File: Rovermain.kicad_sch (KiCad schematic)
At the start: 59 parts, among them J1 48V input, J10 3V3 Output, J11 5V Output, J13 Steering Bus Bar, J14 Drive Bus Bar, J15 Arm Bus Bar, J16 Pi_48V_Ctrl, J17 Spare 48V port, J2 USB_C_Receptacle_Pi_Power, J3 24V Output, J4 USB_C_Receptacle_Spare_power, J5 Buck 48/24, J6 Buck 24/12, J7 Buck 24/5, J8 Buck 12/3v3, J9 12V Output, Q1 Arm ctrl, Q2 Steer ctrl, Q3 Drive ctrl, Q4 Spare ctrl, SW2 SW_Push_Open

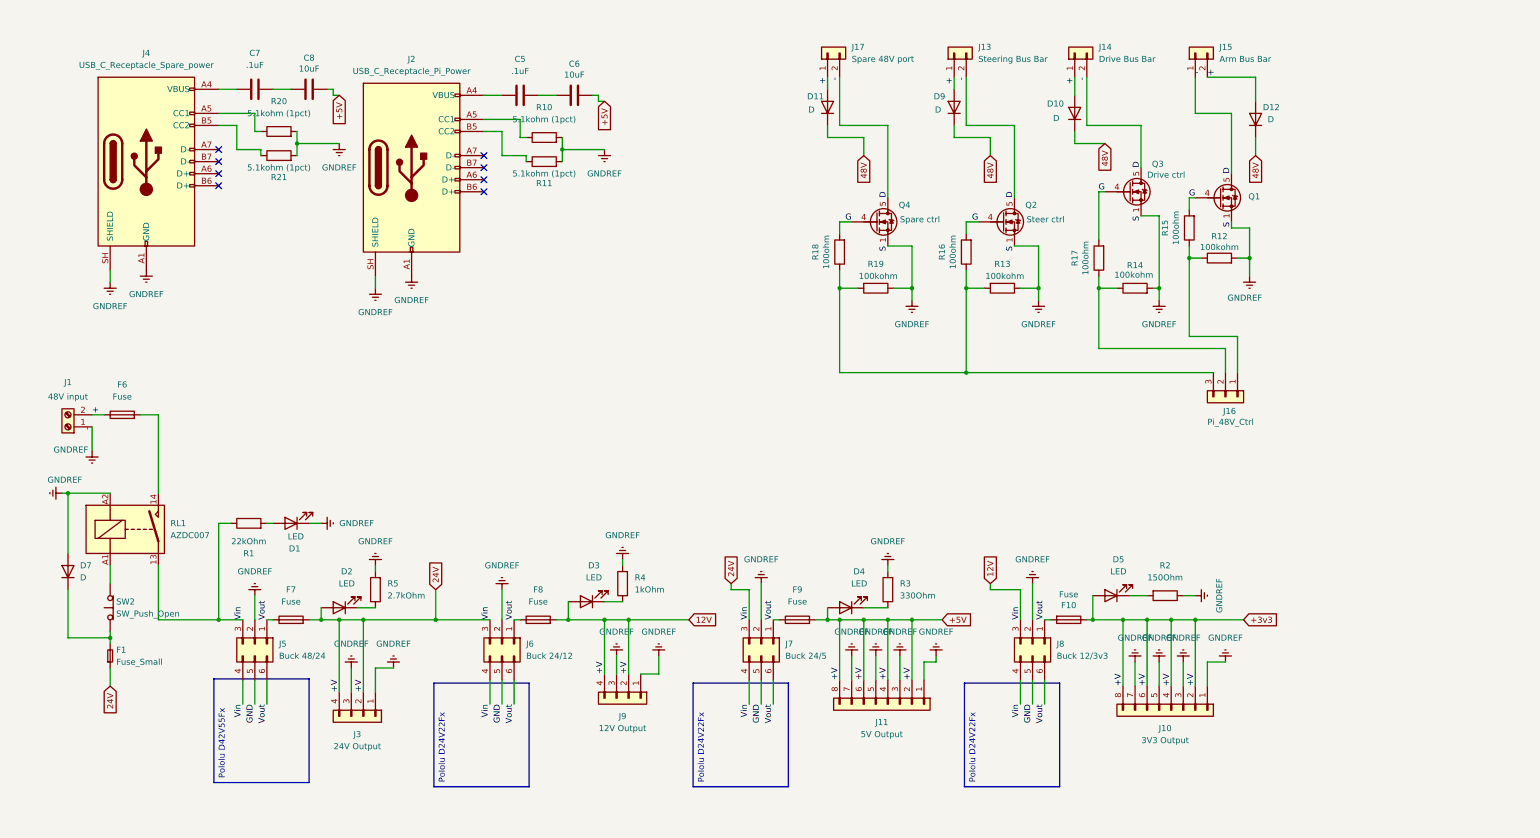
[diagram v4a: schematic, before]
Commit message: finalizing footprints, created layout
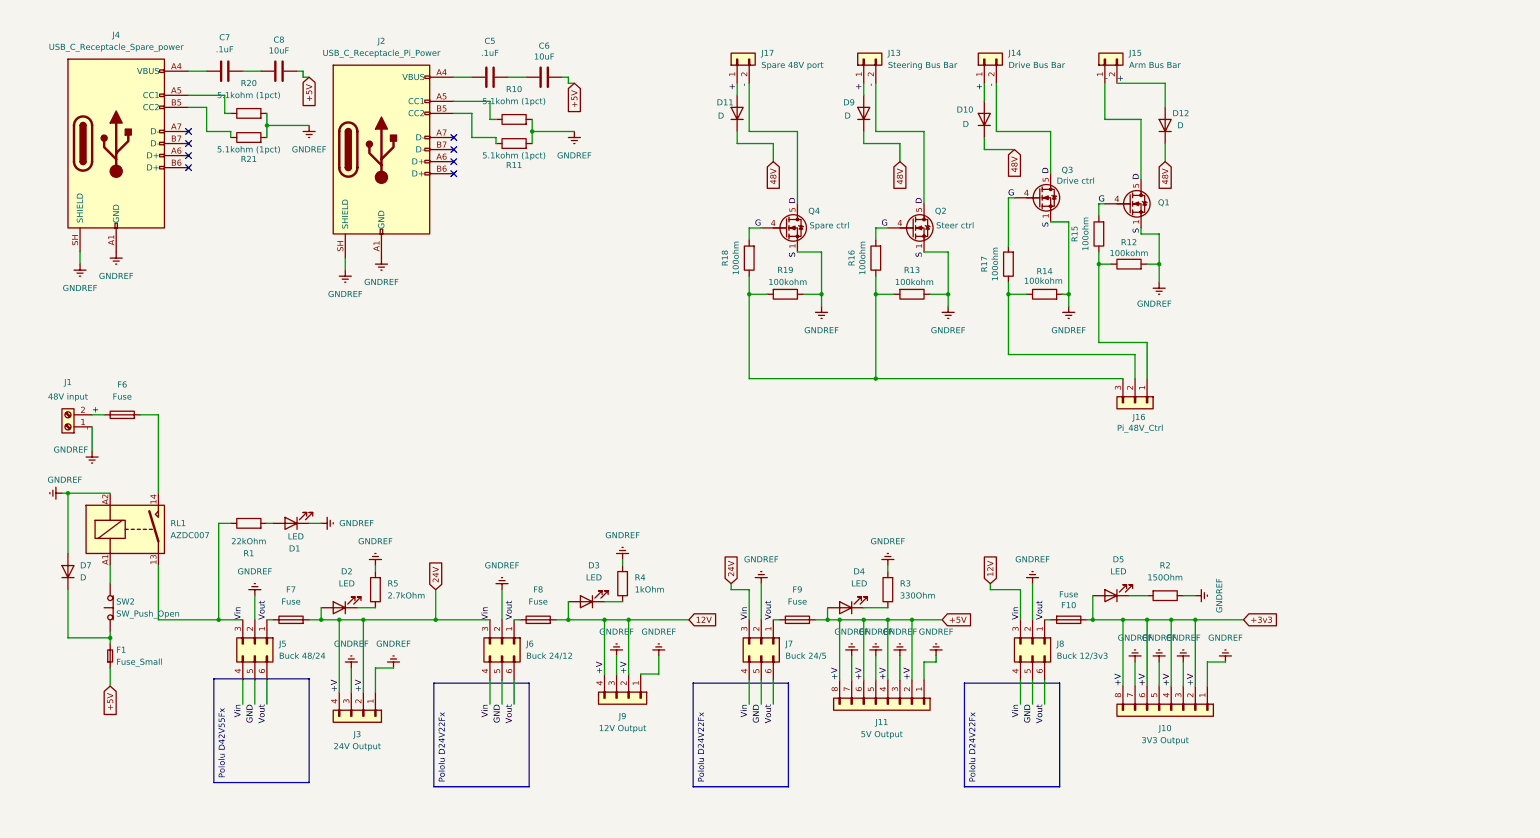
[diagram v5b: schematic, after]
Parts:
- D1, D2, D3, D4, D5: footprint (none) -> LED_SMD:LED_0603_1608Metric
- D7: footprint SM74611KTTR:TO254P1524X483-3N -> Diode_THT:D_DO-41_SOD81_P5.08mm_Vertical_AnodeUp
- F1, F10, F6, F7, F8, F9: footprint (none) -> Fuse:Fuse_0603_1608Metric
- J10, J11: footprint (none) -> TerminalBlock_Phoenix:TerminalBlock_Phoenix_PT-1,5-8-5.0-H_1x08_P5.00mm_Horizontal
- J13, J14, J15, J17: footprint Button_Switch_THT:SW_Slide-03_Wuerth-WS-SLTV_10x2.5x6.4_P2.54mm -> TerminalBlock_Phoenix:TerminalBlock_Phoenix_PT-1,5-2-5.0-H_1x02_P5.00mm_Horizontal
- J16: footprint Button_Switch_THT:SW_Slide-03_Wuerth-WS-SLTV_10x2.5x6.4_P2.54mm -> TerminalBlock_Phoenix:TerminalBlock_Phoenix_PT-1,5-3-5.0-H_1x03_P5.00mm_Horizontal
- J3, J9: footprint (none) -> TerminalBlock_Phoenix:TerminalBlock_Phoenix_PT-1,5-4-5.0-H_1x04_P5.00mm_Horizontal
- J5, J6, J7, J8: footprint (none) -> Phoenix-3PT-1984028:1984028
- R1, R5: footprint Package_DIP:DIP-8_W7.62mm -> Resistor_SMD:R_2512_6332Metric
- R12, R13, R14, R19: footprint Package_DIP:DIP-8_W7.62mm -> Resistor_SMD:R_0402_1005Metric
- R15, R16, R17, R18, R2, R3, R4: footprint Package_DIP:DIP-8_W7.62mm -> Resistor_SMD:R_1206_3216Metric
- SW2: footprint Button_Switch_THT:SW_NKK_GW12LJP -> Button-GPTS2032:SWITCH_03211B
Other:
- moved on the sheet: C5, C6, C7, C8, D10, D11, D12, D9, J13, J14, J15, J16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

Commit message: updated footprints
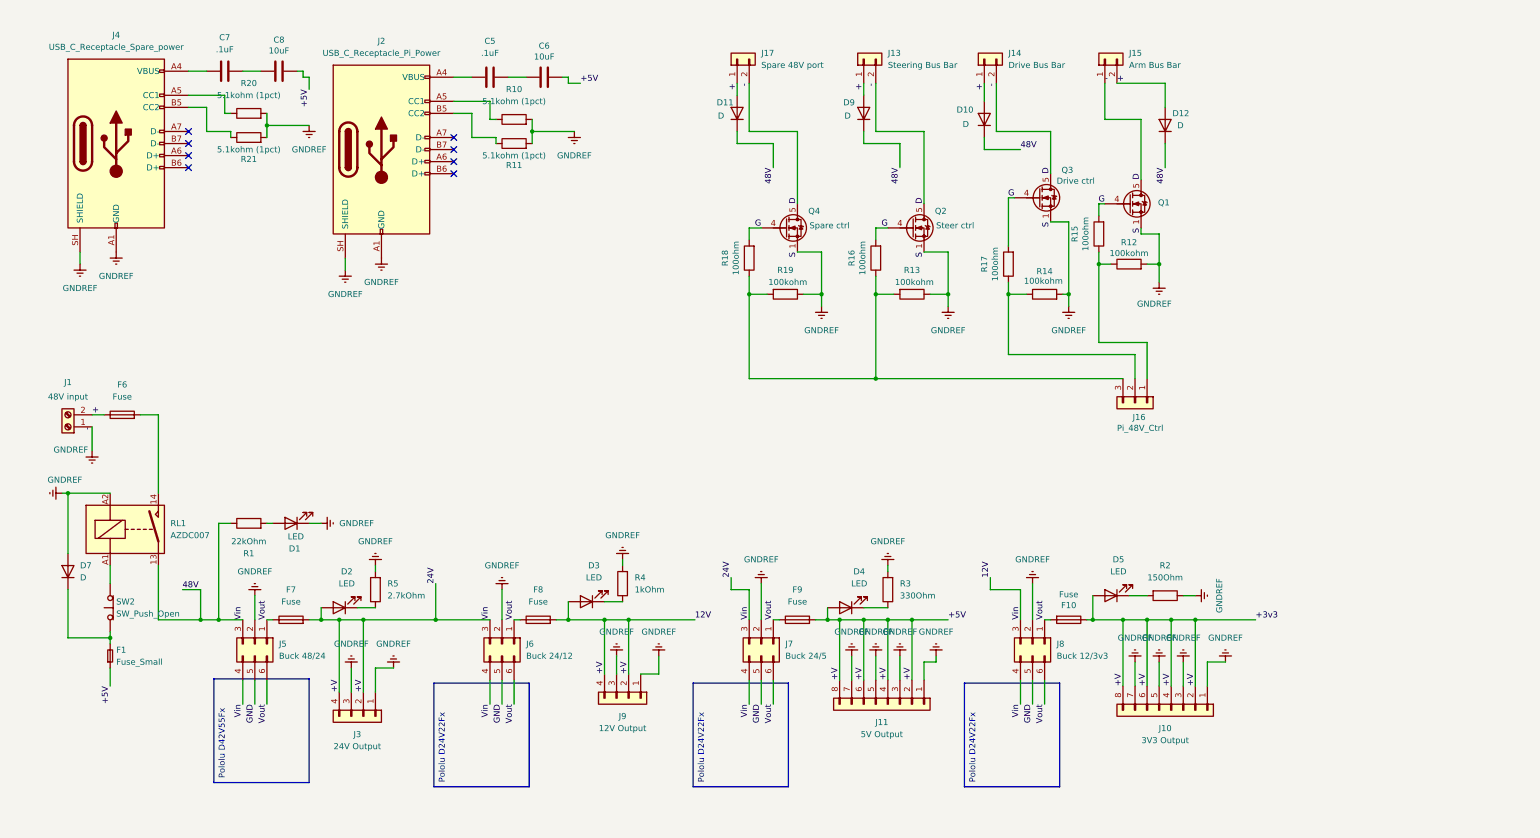
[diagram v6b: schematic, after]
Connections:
- net 48V is gone; now on net +3v3: D10.1 (K), D11.1 (K), D12.1 (K), D9.1 (K)

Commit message: Routing part 1
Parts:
- removed J16: Pi_48V_Ctrl, TerminalBlock_Phoenix:TerminalBlock_Phoenix_PT-1,5-3-5.0-H_1x03_P5.00mm_Horizontal, symbol Connector_Generic:Conn_01x03
- removed J5: Buck 48/24, Phoenix-3PT-1984028:1984028, symbol Connector_Generic:Conn_02x03_Counter_Clockwise
- removed J6: Buck 24/12, Phoenix-3PT-1984028:1984028, symbol Connector_Generic:Conn_02x03_Counter_Clockwise
- removed J7: Buck 24/5, Phoenix-3PT-1984028:1984028, symbol Connector_Generic:Conn_02x03_Counter_Clockwise
- removed J8: Buck 12/3v3, Phoenix-3PT-1984028:1984028, symbol Connector_Generic:Conn_02x03_Counter_Clockwise
- added J12: Pi_48V_Control, TerminalBlock_Phoenix:TerminalBlock_Phoenix_PT-1,5-4-5.0-H_1x04_P5.00mm_Horizontal, symbol Connector_Generic:Conn_01x04
- added J5: Buck 48/24, TerminalBlock_Phoenix:TerminalBlock_Phoenix_PT-1,5-3-5.0-H_1x03_P5.00mm_Horizontal, symbol Connector_Generic:Conn_01x03
- added J6: Buck 24/12, TerminalBlock_Phoenix:TerminalBlock_Phoenix_PT-1,5-3-5.0-H_1x03_P5.00mm_Horizontal, symbol Connector_Generic:Conn_01x03
- added J7: Buck 24/5, TerminalBlock_Phoenix:TerminalBlock_Phoenix_PT-1,5-3-5.0-H_1x03_P5.00mm_Horizontal, symbol Connector_Generic:Conn_01x03
- added J8: Buck 12/3V3, TerminalBlock_Phoenix:TerminalBlock_Phoenix_PT-1,5-3-5.0-H_1x03_P5.00mm_Horizontal, symbol Connector_Generic:Conn_01x03
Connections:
- net +3v3: no longer C6.1, C8.1, D10.1 (K), D11.1 (K), D12.1 (K), D2.2 (A), D3.2 (A), D4.2 (A), D9.1 (K), F1.1, F7.2, F8.2, F9.2, J11.2 (Pin_2), J11.4 (Pin_4), J11.6 (Pin_6), J11.8 (Pin_8), J3.2 (Pin_2), J3.4 (Pin_4), J9.2 (Pin_2), J9.4 (Pin_4), R1.1, RL1.13
- net GNDREF: now also J5.2 (Pin_2), J6.2 (Pin_2), J7.2 (Pin_2), J8.2 (Pin_2); no longer J13.2 (Pin_2), J14.2 (Pin_2), J15.1 (Pin_1), J17.2 (Pin_2), Q1.5 (D), Q2.5 (D), Q3.5 (D), Q4.5 (D)
- net at R18.1, R19.2: now also J12.4 (Pin_4); no longer R13.2, R16.1
- net at R14.1, R17.1: now also J12.2 (Pin_2)
- net at R12.1, R15.1: now also J12.1 (Pin_1)
- removed net +: D10.2 (A), D11.2 (A), D12.2 (A), D9.2 (A), F6.1, J1.2 (Pin_2), J13.1 (Pin_1), J14.1 (Pin_1), J15.2 (Pin_2), J17.1 (Pin_1)
- removed net G: Q1.4 (G), Q2.4 (G), Q3.4 (G), Q4.4 (G), R15.2, R16.2, R17.2, R18.2
- removed net Vout: F10.2, F7.1, F8.1, F9.1
- new net: F8.1, J6.1 (Pin_1)
- new net: F6.1, J1.2 (Pin_2)
- new net: Q4.4 (G), R18.2
- new net: J17.2 (Pin_2), Q4.5 (D)
- new net: D11.2 (A), J17.1 (Pin_1)
- new net: D9.2 (A), J13.1 (Pin_1)
- new net: J12.3 (Pin_3), R13.2, R16.1
- new net: D10.2 (A), J14.1 (Pin_1)
- new net: J14.2 (Pin_2), Q3.5 (D)
- new net: F7.1, J5.1 (Pin_1)
- new net: Q3.4 (G), R17.2
- new net: D12.2 (A), J15.2 (Pin_2)
- new net: J13.2 (Pin_2), Q2.5 (D)
- new net: J15.1 (Pin_1), Q1.5 (D)
- new net: Q1.4 (G), R15.2
- new net: F10.2, J8.1 (Pin_1)
- new net: F9.1, J7.1 (Pin_1)
- new net: Q2.4 (G), R16.2
- new net +5V: C6.1, C8.1, D4.2 (A), F1.1, F9.2, J11.2 (Pin_2), J11.4 (Pin_4), J11.6 (Pin_6), J11.8 (Pin_8)
- new net 12V: D3.2 (A), F8.2, J8.3 (Pin_3), J9.2 (Pin_2), J9.4 (Pin_4)
- new net 24V: D2.2 (A), F7.2, J3.2 (Pin_2), J3.4 (Pin_4), J6.3 (Pin_3), J7.3 (Pin_3)
- new net 48V: D10.1 (K), D11.1 (K), D12.1 (K), D9.1 (K), J5.3 (Pin_3), R1.1, RL1.13

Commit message: Routed everything but GNDs
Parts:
- J2, J4: footprint Module:Arduino_UNO_R2 -> USB-C-PD-2171750001:2171750001_MOL
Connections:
- net +5V: now also C5.1, C6.2, C7.1, C8.2, J2.A4 (VBUS), J2.A9 (VBUS), J2.B4 (VBUS), J2.B9 (VBUS), J4.A4 (VBUS), J4.A9 (VBUS), J4.B4 (VBUS), J4.B9 (VBUS); no longer C6.1, C8.1
- net GNDREF: now also C5.2, C6.1, C7.2, C8.1
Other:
- moved on the sheet: C6, C7
